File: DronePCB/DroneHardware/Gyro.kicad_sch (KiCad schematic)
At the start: 4 parts, among them U301 MPU-6000

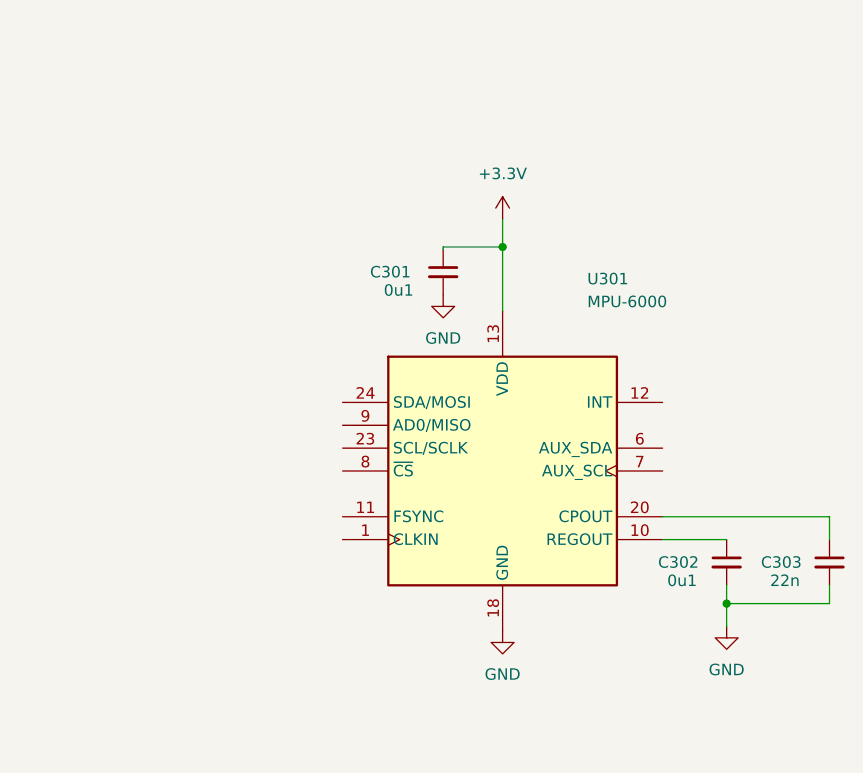
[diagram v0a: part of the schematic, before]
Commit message: Aggiornamento Aggiunta della MPU-6050 per test
E' stato fatto uno studio per capire il funzionamento di OMNIBUSF4
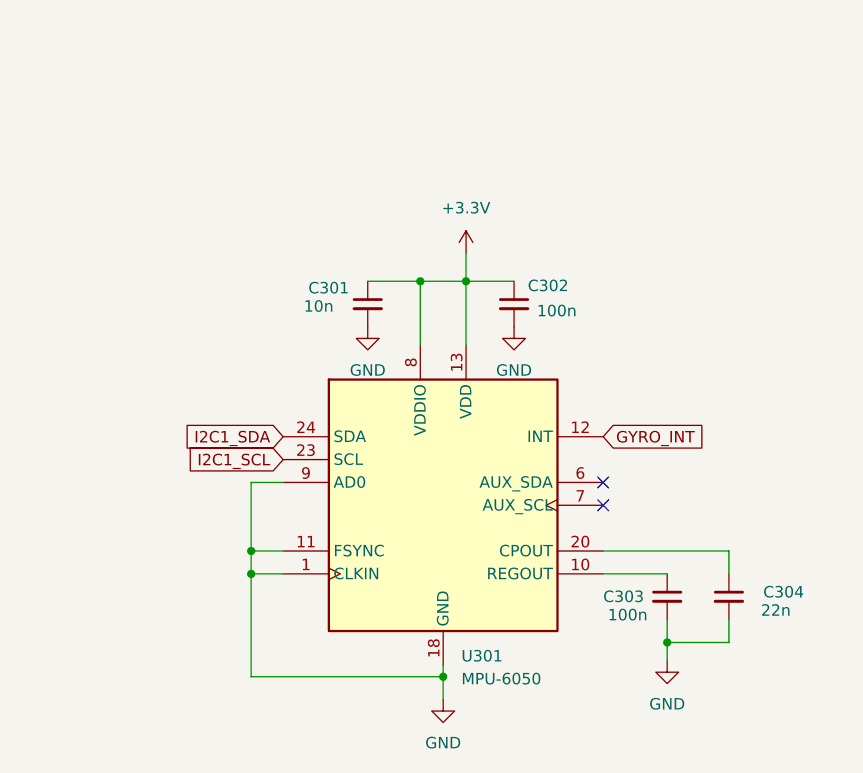
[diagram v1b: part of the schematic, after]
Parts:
- removed C302: 0u1, Capacitor_SMD:C_0402_1005Metric, symbol Device:C_Small
- removed U301: MPU-6000, Sensor_Motion:InvenSense_QFN-24_4x4mm_P0.5mm, symbol Sensor_Motion:MPU-6000
- added C301: 10n, Capacitor_SMD:C_0402_1005Metric, symbol Device:C_Small
- added C304: 22n, Capacitor_SMD:C_0402_1005Metric, symbol Device:C_Small
- added U301: MPU-6050, Sensor_Motion:InvenSense_QFN-24_4x4mm_P0.5mm, symbol Sensor_Motion:MPU-6050
- C302: renamed from C301; value 0u1 -> 100n
- C303: value 22n -> 100n
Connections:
- net +3V3: now also C301.1, U301.13 (VDD), U301.8 (VDDIO)
- net GND: now also C301.2, C304.2, U301.1 (CLKIN), U301.11 (FSYNC), U301.18 (GND), U301.9 (AD0)
- net at C303.1: now also U301.10 (REGOUT)
- new net: C304.1, U301.20 (CPOUT)
- new net GYRO_INT: U301.12 (INT)
- new net I2C1_SCL: U301.23 (SCL)
- new net I2C1_SDA: U301.24 (SDA)
- no-connect marks 0 -> 2
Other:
- moved on the sheet: C302

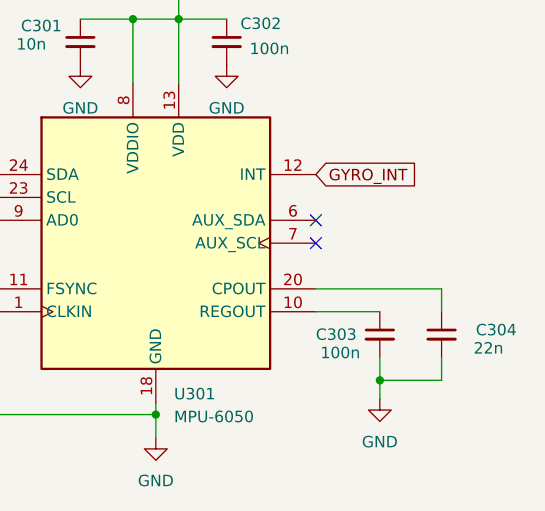
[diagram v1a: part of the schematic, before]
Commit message: Creazione PCB e utilizzo di processore STM32F405
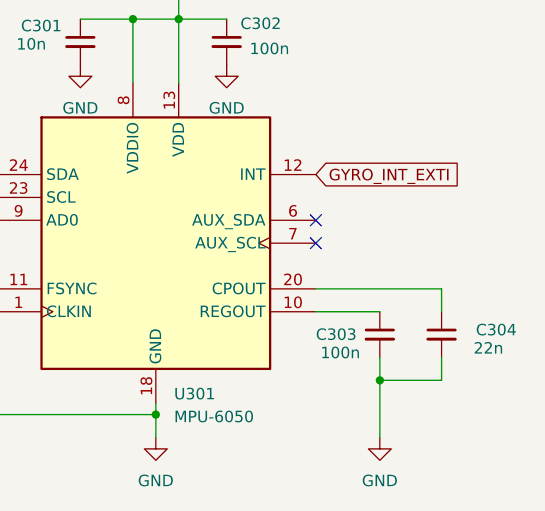
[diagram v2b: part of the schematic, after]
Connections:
- net GYRO_INT renamed GYRO_INT_EXTI
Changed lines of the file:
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@@
     (stroke (width 0) (type default) (color 0 0 0 0))
   )
-  (wire (pts (xy 166.37 113.03) (xy 166.37 115.062))
+  (wire (pts (xy 166.37 113.03) (xy 166.37 119.38))
     (stroke (width 0) (type default) (color 0 0 0 0))
   )
@@
     (effects (font (size 1.27 1.27)) (justify left bottom))
   )
-  (global_label "GYRO_INT" (shape input) (at 159.258 90.17 0) (fields_autoplaced)
+  (global_label "GYRO_INT_EXTI" (shape input) (at 159.258 90.17 0) (fields_autoplaced)
     (effects (font (size 1.27 1.27)) (justify left))
-    (property "Intersheet References" "${INTERSHEET_REFS}" (id 0) (at 170.5006 90.0906 0)
+    (property "Intersheet References" "${INTERSHEET_REFS}" (id 0) (at 175.3992 90.2494 0)
       (effects (font (size 1.27 1.27)) (justify left) hide)
     )
@@
     (pin "1")
   )
-  (symbol (lib_id "power:GND") (at 166.37 115.062 0) (unit 1)
+  (symbol (lib_id "power:GND") (at 166.37 119.38 0) (unit 1)
     (in_bom yes) (on_board yes) (fields_autoplaced)
-    (property "Reference" "#PWR0305" (id 0) (at 166.37 121.412 0)
+    (property "Reference" "#PWR0305" (id 0) (at 166.37 125.73 0)
       (effects (font (size 1.27 1.27)) hide)
     )
-    (property "Value" "GND" (id 1) (at 166.37 119.888 0))
-    (property "Footprint" "" (id 2) (at 166.37 115.062 0)
+    (property "Value" "GND" (id 1) (at 166.37 124.206 0))
+    (property "Footprint" "" (id 2) (at 166.37 119.38 0)
       (effects (font (size 1.27 1.27)) hide)
     )
-    (property "Datasheet" "" (id 3) (at 166.37 115.062 0)
+    (property "Datasheet" "" (id 3) (at 166.37 119.38 0)
       (effects (font (size 1.27 1.27)) hide)
     )

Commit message: Utilizzo di mpu-6000
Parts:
- removed C304: 22n, Capacitor_SMD:C_0402_1005Metric, symbol Device:C_Small
- removed U301: MPU-6050, Sensor_Motion:InvenSense_QFN-24_4x4mm_P0.5mm, symbol Sensor_Motion:MPU-6050
- added U301: MPU-6000, Sensor_Motion:InvenSense_QFN-24_4x4mm_P0.5mm, symbol Sensor_Motion:MPU-6000
- C301: value 10n -> 100n
- C303: value 100n -> 22n
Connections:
- net +3V3: now also U301.13 (VDD); no longer C302.1
- net GND: now also U301.1 (CLKIN), U301.11 (FSYNC), U301.18 (GND), U301.8 (~{CS}), U301.9 (AD0/MISO)
- net GYRO_INT_EXTI: now also U301.12 (INT)
- net I2C1_SCL: now also U301.23 (SCL/SCLK)
- net I2C1_SDA: now also U301.24 (SDA/MOSI)
- net at C303.1: now also U301.20 (CPOUT)
- new net: C302.1, U301.10 (REGOUT)

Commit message: Da eliminare
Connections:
- net GND: no longer U301.8 (~{CS})
- new net MPU6000_CS_PIN: U301.8 (~{CS})
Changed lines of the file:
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@@
   (junction (at 171.196 116.078) (diameter 0) (color 0 0 0 0)
-  )
-  (junction (at 124.968 103.378) (diameter 0) (color 0 0 0 0)
   )
   (junction (at 146.304 75.946) (diameter 0) (color 0 0 0 0)
@@
   )
   (wire (pts (xy 124.968 103.378) (xy 124.968 105.918))
-    (stroke (width 0) (type default) (color 0 0 0 0))
-  )
-  (wire (pts (xy 124.968 100.838) (xy 124.968 103.378))
-    (stroke (width 0) (type default) (color 0 0 0 0))
-  )
-  (wire (pts (xy 124.968 100.838) (xy 128.524 100.838))
     (stroke (width 0) (type default) (color 0 0 0 0))
   )
@@
       (effects (font (size 1.27 1.27)) (justify right) hide)
     )
+  )
+  (global_label "MPU6000_CS_PIN" (shape input) (at 128.524 100.838 180) (fields_autoplaced)
+    (effects (font (size 1.27 1.27)) (justify right))
+    (property "Intersheet References" "${INTERSHEET_REFS}" (id 0) (at 109.6009 100.9174 0)
+      (effects (font (size 1.27 1.27)) (justify right) hide)
+    )

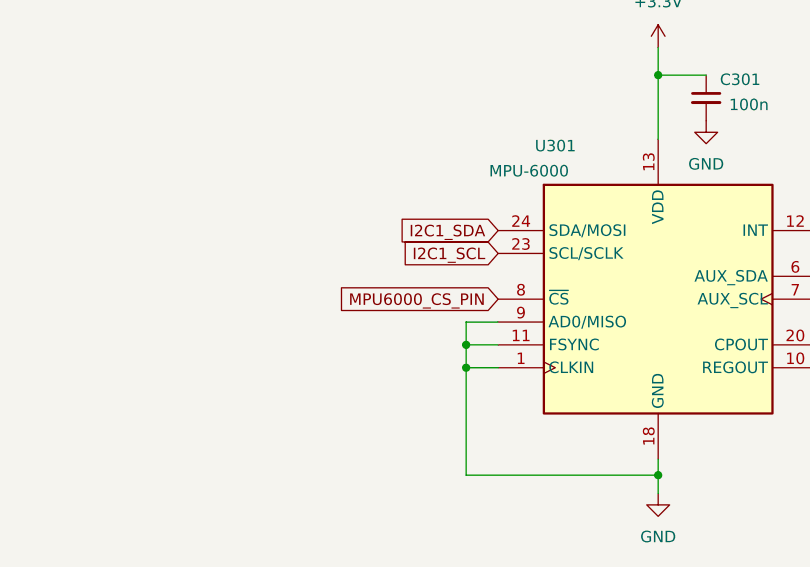
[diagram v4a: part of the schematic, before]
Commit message: Collegamento corretto di mpu-6000
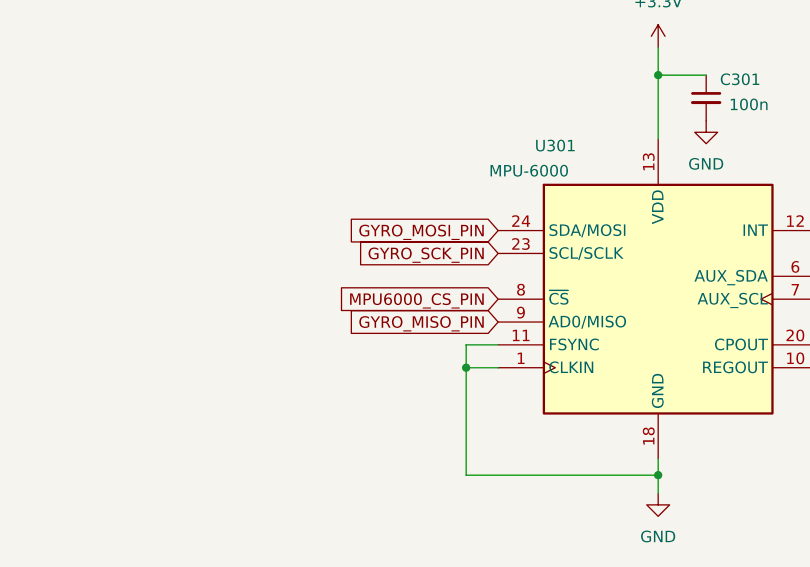
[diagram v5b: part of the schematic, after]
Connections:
- net GND: no longer U301.9 (AD0/MISO)
- net I2C1_SCL renamed GYRO_SCK_PIN
- net I2C1_SDA renamed GYRO_MOSI_PIN
- new net GYRO_MISO_PIN: U301.9 (AD0/MISO)
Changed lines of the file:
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@@
   (junction (at 146.304 120.396) (diameter 0) (color 0 0 0 0)
-  )
-  (junction (at 124.968 105.918) (diameter 0) (color 0 0 0 0)
   )
   (no_connect (at 164.084 100.838))
   (no_connect (at 164.084 98.298))
   (wire (pts (xy 178.054 105.918) (xy 178.054 108.458))
-    (stroke (width 0) (type default) (color 0 0 0 0))
-  )
-  (wire (pts (xy 124.968 103.378) (xy 124.968 105.918))
     (stroke (width 0) (type default) (color 0 0 0 0))
   )
@@
   )
   (wire (pts (xy 124.968 120.396) (xy 146.304 120.396))
-    (stroke (width 0) (type default) (color 0 0 0 0))
-  )
-  (wire (pts (xy 124.968 103.378) (xy 128.524 103.378))
     (stroke (width 0) (type default) (color 0 0 0 0))
   )
@@
     (effects (font (size 1.27 1.27)) (justify left bottom))
   )
-  (global_label "I2C1_SDA" (shape input) (at 128.524 93.218 180) (fields_autoplaced)
+  (global_label "GYRO_SCK_PIN" (shape input) (at 128.524 95.758 180) (fields_autoplaced)
     (effects (font (size 1.27 1.27)) (justify right))
-    (property "Intersheet References" "${INTERSHEET_REFS}" (id 0) (at 117.2814 93.2974 0)
+    (property "Intersheet References" "${INTERSHEET_REFS}" (id 0) (at 112.2619 95.8374 0)
       (effects (font (size 1.27 1.27)) (justify right) hide)
     )
   )
-  (global_label "I2C1_SCL" (shape input) (at 128.524 95.758 180) (fields_autoplaced)
+  (global_label "GYRO_MISO_PIN" (shape input) (at 128.524 103.378 180) (fields_autoplaced)
     (effects (font (size 1.27 1.27)) (justify right))
-    (property "Intersheet References" "${INTERSHEET_REFS}" (id 0) (at 117.3419 95.8374 0)
+    (property "Intersheet References" "${INTERSHEET_REFS}" (id 0) (at 111.4152 103.4574 0)
       (effects (font (size 1.27 1.27)) (justify right) hide)
     )
+  )
+  (global_label "GYRO_MOSI_PIN" (shape input) (at 128.524 93.218 180) (fields_autoplaced)
+    (effects (font (size 1.27 1.27)) (justify right))
+    (property "Intersheet References" "${INTERSHEET_REFS}" (id 0) (at 111.4152 93.2974 0)
+      (effects (font (size 1.27 1.27)) (justify right) hide)
+    )
